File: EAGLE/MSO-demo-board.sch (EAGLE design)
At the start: 43 parts, among them IC1 ATMEGA168-20P, J1 AVR_SPI_PRG_62X3_LOCK

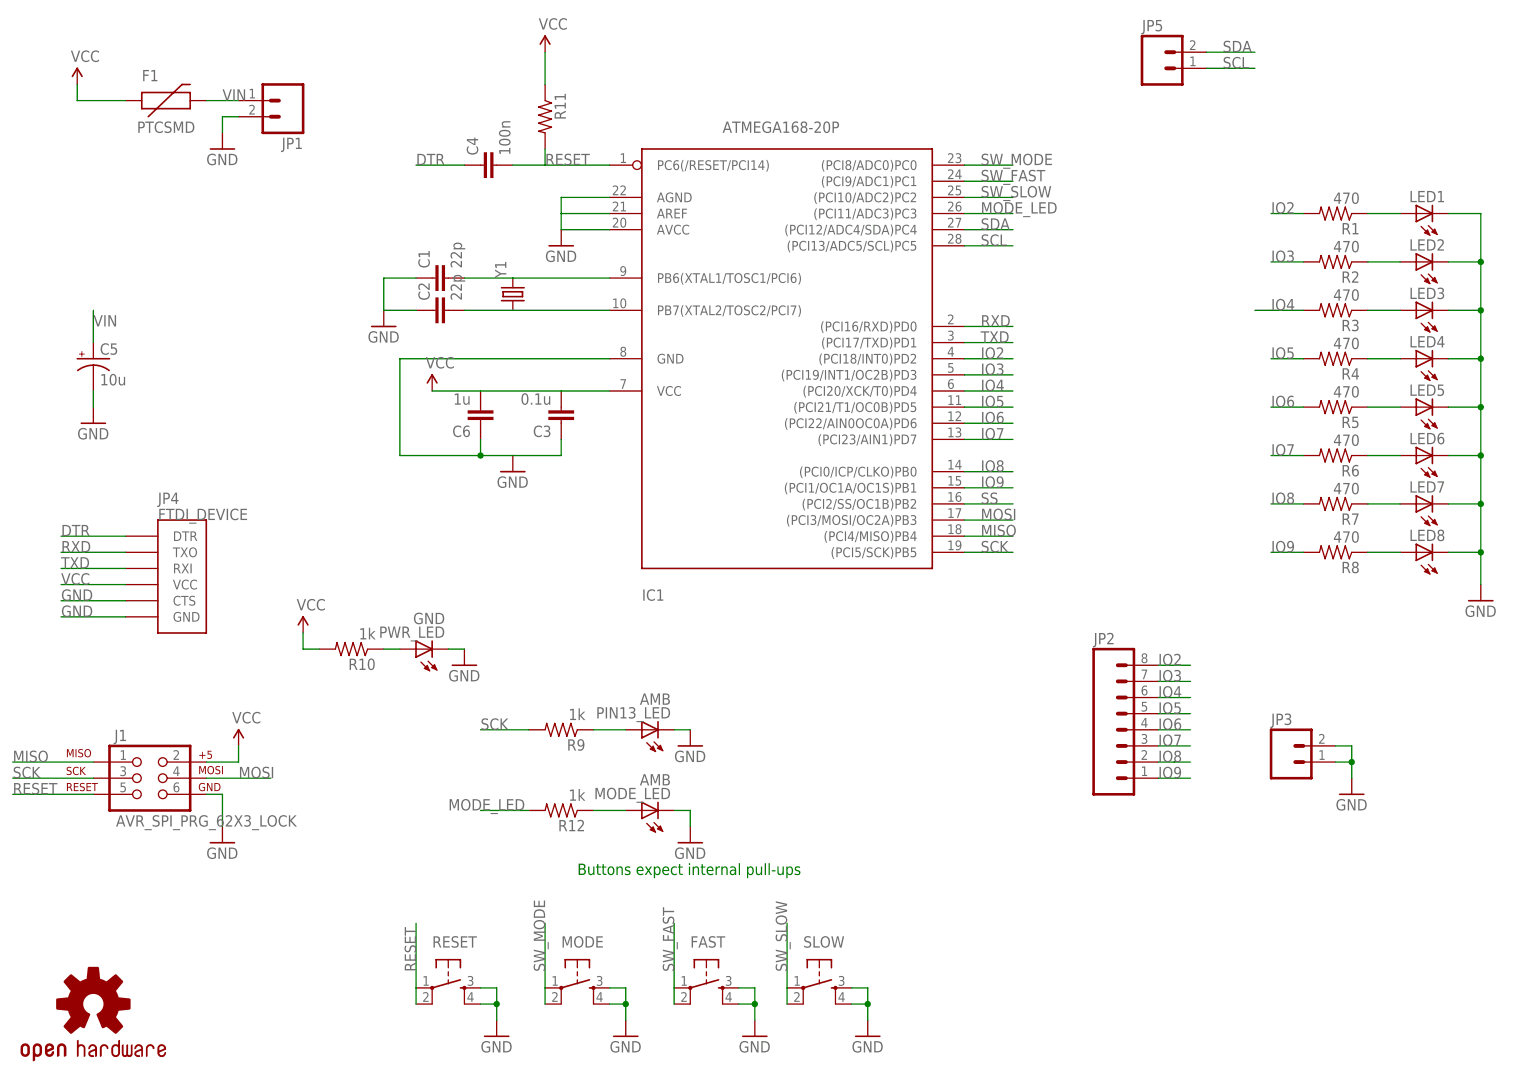
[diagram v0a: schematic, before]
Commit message: Fixed VCC Grounded mistake
AVCC was tied to ground causing a short at power up.  Tied AVCC and
AREF to 5V instead of ground.  Also swapped TX and RX on FTDI pinout
(was backwards)
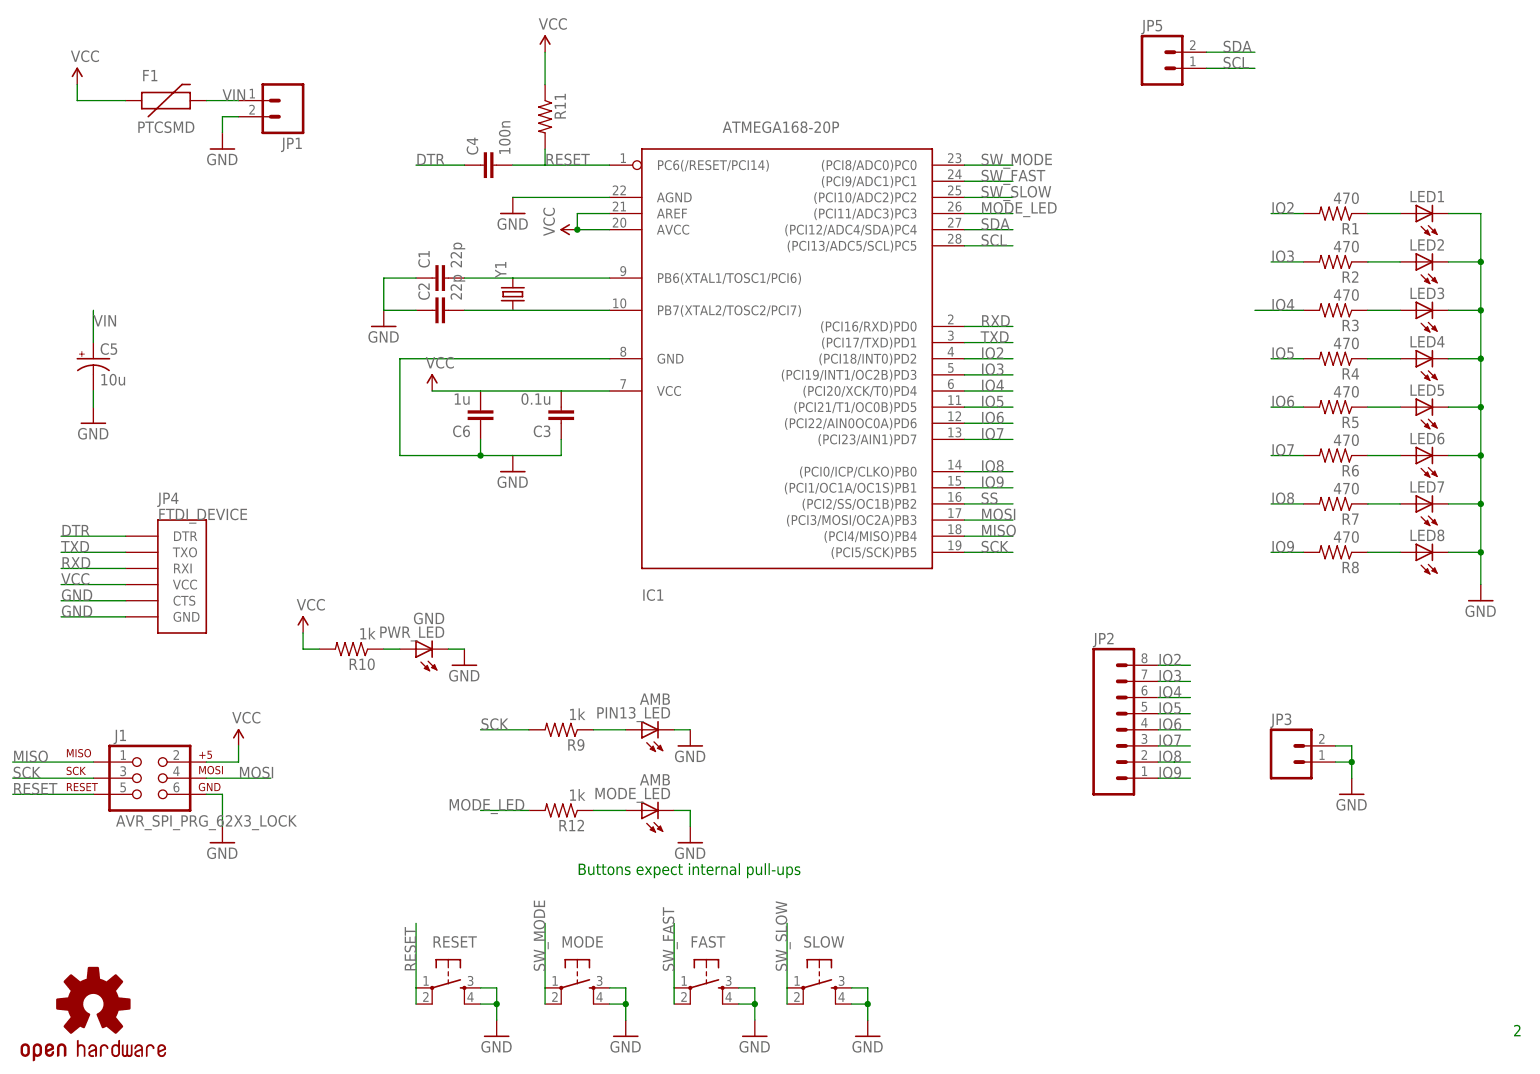
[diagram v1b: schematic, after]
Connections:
- net GND: no longer IC1.AREF, IC1.AVCC
- net RXD: now also JP4.RXI; no longer JP4.TXO
- net TXD: now also JP4.TXO; no longer JP4.RXI
- net VCC: now also IC1.AREF, IC1.AVCC
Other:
- note added: "2"
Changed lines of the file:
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@@
 <part name="GND15" library="SparkFun" deviceset="GND" device=""/>
 <part name="U$1" library="Add-Ohms" deviceset="OSHW-LOGO" device="S"/>
+<part name="P+1" library="SparkFun" deviceset="VCC" device=""/>
 </parts>
 <sheets>
@@
 <plain>
 <text x="93.98" y="33.02" size="1.778" layer="91">Buttons expect internal pull-ups</text>
+<text x="241.3" y="7.62" size="1.778" layer="91">2</text>
 </plain>
 <instances>
@@
 <instance part="GND5" gate="1" x="76.2" y="66.04"/>
 <instance part="GND6" gate="1" x="63.5" y="119.38"/>
-<instance part="GND7" gate="1" x="91.44" y="132.08"/>
+<instance part="GND7" gate="1" x="83.82" y="137.16"/>
 <instance part="GND8" gate="1" x="38.1" y="147.32"/>
 <instance part="GND9" gate="1" x="38.1" y="38.1"/>
@@
 <instance part="GND15" gate="1" x="111.76" y="38.1"/>
 <instance part="U$1" gate="G$1" x="17.78" y="12.7"/>
+<instance part="P+1" gate="1" x="93.98" y="134.62" rot="R90"/>
 </instances>
 <busses>
@@
 <pinref part="IC1" gate="G$1" pin="AGND"/>
 <pinref part="GND7" gate="1" pin="GND"/>
-<wire x1="99.06" y1="139.7" x2="91.44" y2="139.7" width="0.1524" layer="91"/>
-<wire x1="91.44" y1="139.7" x2="91.44" y2="137.16" width="0.1524" layer="91"/>
-<pinref part="IC1" gate="G$1" pin="AREF"/>
-<wire x1="91.44" y1="137.16" x2="91.44" y2="134.62" width="0.1524" layer="91"/>
-<wire x1="99.06" y1="137.16" x2="91.44" y2="137.16" width="0.1524" layer="91"/>
-<pinref part="IC1" gate="G$1" pin="AVCC"/>
-<wire x1="99.06" y1="134.62" x2="91.44" y2="134.62" width="0.1524" layer="91"/>
+<wire x1="99.06" y1="139.7" x2="83.82" y2="139.7" width="0.1524" layer="91"/>
 </segment>
 <segment>
@@
 <label x="12.7" y="78.74" size="1.778" layer="95"/>
 </segment>
+<segment>
+<pinref part="IC1" gate="G$1" pin="AREF"/>
+<wire x1="99.06" y1="137.16" x2="93.98" y2="137.16" width="0.1524" layer="91"/>
+<wire x1="93.98" y1="137.16" x2="93.98" y2="134.62" width="0.1524" layer="91"/>
+<pinref part="IC1" gate="G$1" pin="AVCC"/>
+<wire x1="93.98" y1="134.62" x2="99.06" y2="134.62" width="0.1524" layer="91"/>
+<pinref part="P+1" gate="1" pin="VCC"/>
+<junction x="93.98" y="134.62"/>
+</segment>
 </net>
 <net name="RESET" class="0">
@@
 </segment>
 <segment>
+<pinref part="JP4" gate="G$1" pin="RXI"/>
+<wire x1="22.86" y1="81.28" x2="12.7" y2="81.28" width="0.1524" layer="91"/>
+<label x="12.7" y="81.28" size="1.778" layer="95"/>
+</segment>
+</net>
+<net name="TXD" class="0">
+<segment>
+<pinref part="IC1" gate="G$1" pin="(PCI17/TXD)PD1"/>
+<wire x1="154.94" y1="116.84" x2="162.56" y2="116.84" width="0.1524" layer="91"/>
+<label x="157.48" y="116.84" size="1.778" layer="95"/>
+</segment>
+<segment>
 <pinref part="JP4" gate="G$1" pin="TXO"/>
 <wire x1="22.86" y1="83.82" x2="12.7" y2="83.82" width="0.1524" layer="91"/>
@@
 </segment>
 </net>
-<net name="TXD" class="0">
-<segment>
-<pinref part="IC1" gate="G$1" pin="(PCI17/TXD)PD1"/>
-<wire x1="154.94" y1="116.84" x2="162.56" y2="116.84" width="0.1524" layer="91"/>
-<label x="157.48" y="116.84" size="1.778" layer="95"/>
-</segment>
-<segment>
-<pinref part="JP4" gate="G$1" pin="RXI"/>
-<wire x1="22.86" y1="81.28" x2="12.7" y2="81.28" width="0.1524" layer="91"/>
-<label x="12.7" y="81.28" size="1.778" layer="95"/>
-</segment>
-</net>
